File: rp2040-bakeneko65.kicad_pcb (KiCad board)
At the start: 2 copper layers, 303.8 x 94.2 mm, 188 parts, among them J1 SM04B-SRSS-TB, SW1 1u, SW10 1u, SW11 1u, SW12 1u, SW13 1u, SW14 1u, SW15 1u, SW16 1u, SW17 2u, SW18 1.5u, SW19 1u, SW2 1u, SW20 1u, SW21 1u, SW22 1u, SW23 1u, SW24 1u, SW25 1u, SW26 1u, SW27 1u, SW28 1u, SW29 1u, SW3 1u, SW30 1u, SW31 1.5u, SW32 ISO Enter, SW33 1u, SW34 1.25u, SW35 1.75u, SW36 1u, SW37 1u, SW38 1u, SW39 1u, SW4 1u, SW40 1u, SW41 1u, SW42 1u, SW43 1u, SW44 1u, SW45 1u, SW46 1u, SW47 2.25u, SW48 1u, SW49 1u, SW5 1u, SW50 2.25u, SW51 1.25u, SW52 1u, SW53 1u, SW54 1u, SW55 1u, SW56 1u, SW57 1u, SW58 1u, SW59 1u, SW6 1u, SW60 1u, SW61 1u, SW62 1u, SW63 1.75u, SW64 1u, SW65 1u, SW66 1.5u, SW67 1.25u, SW68 1u, SW69 1.25u, SW7 1u, SW70 1.5u, SW71 1.25u, SW72 3u, SW73 7u, SW74 6.25u, SW75 3u, SW76 1.25u, SW77 1.5u, SW78 1.25u, SW79 1u, SW8 1u, SW80 1u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

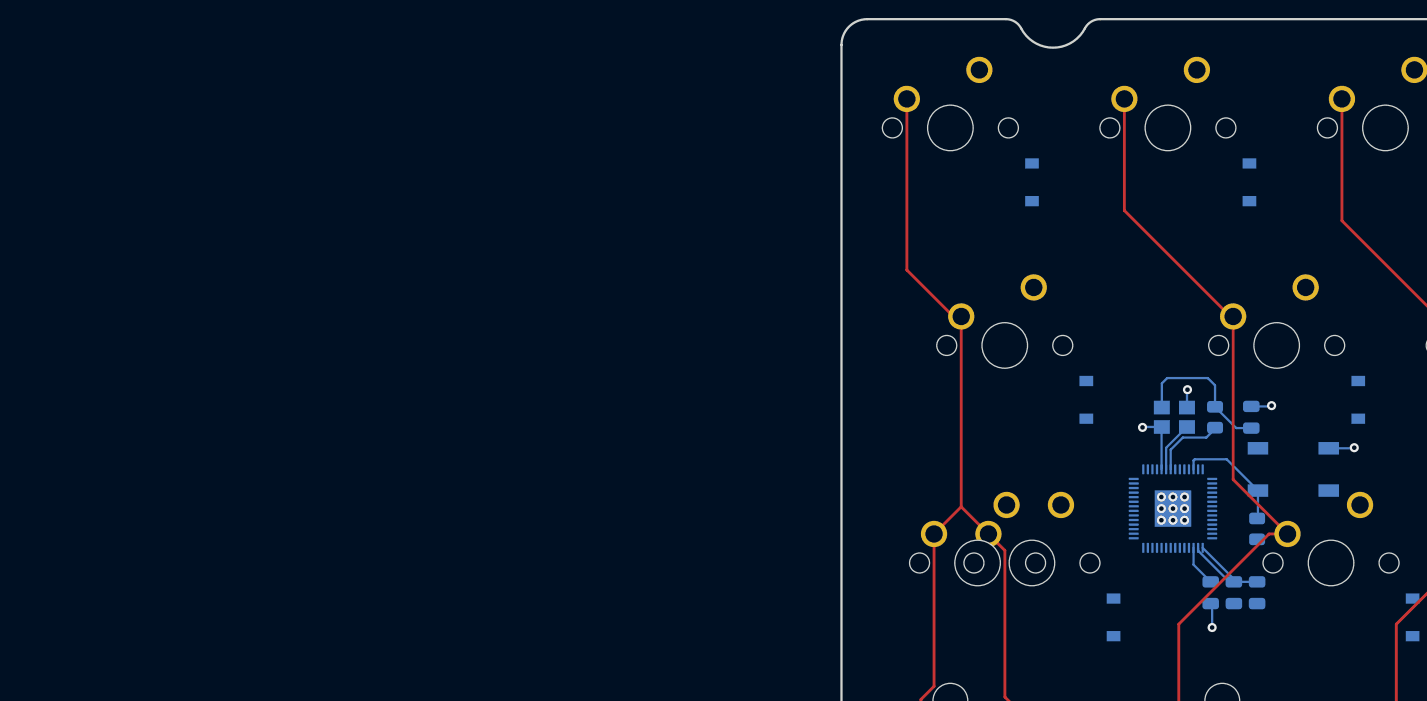
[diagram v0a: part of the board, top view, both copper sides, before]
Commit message: starting over on MCU routing
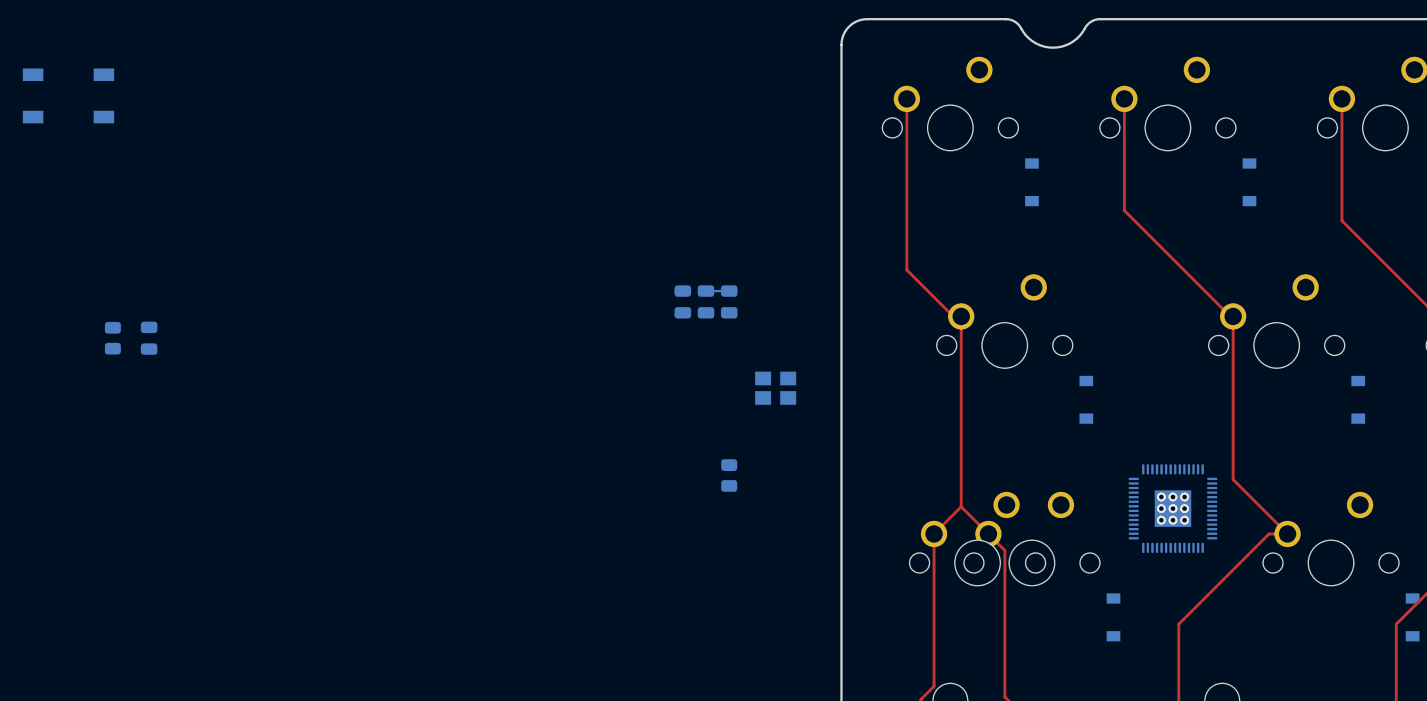
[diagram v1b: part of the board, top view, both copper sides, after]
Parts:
- moved SW83 112.1 mm to (-24.8, 97.2)
- moved C3 96.8 mm to (-17.8, 118.4)
- moved R4 96.8 mm to (-21.0, 118.4)
- moved C11 52.8 mm to (33.0, 115.2)
- moved C10 52.8 mm to (31.0, 115.2)
- moved C6 52.8 mm to (29.0, 115.2)
- moved R3 46.5 mm to (33.0, 130.5)
- moved Y1 35.0 mm to (37.1, 122.8)
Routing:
- net GND: track 14.1 -> 0.00 mm, vias 14 -> 9
- net Net-(C3-Pad2): track 13.3 -> 0.00 mm
- net Net-(R3-Pad2): track 10.2 -> 0.03 mm
- net +3V3: track 10.6 -> 2.44 mm
- net XTAL_OUT: track 6.46 -> 0.00 mm
- net XTAL_IN: track 4.47 -> 0.00 mm
- net +1V1: track 3.60 -> 0.00 mm

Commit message: Use smaller caps and resistors
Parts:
- C1, C10, C11, C12, C13, C14, C15, C16, C17, C2, C3, C4, C5, C6, C7, C8, C9: footprint Capacitor_SMD:C_0805_2012Metric -> Capacitor_SMD:C_0402_1005Metric
- R1, R2, R3, R4: footprint Resistor_SMD:R_0805_2012Metric -> Resistor_SMD:R_0402_1005Metric
- moved R3 60.7 mm to (-24.1, 110.0)
- moved C3 46.1 mm to (27.9, 124.4)
- moved R4 6.64 mm to (-27.6, 119.1)

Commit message: Reposition crystal
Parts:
- moved C2 414.5 mm to (75.9, 139.4), turned to -90 degrees
- moved R4 98.8 mm to (69.1, 139.4), turned to 90 degrees
- moved Y1 39.5 mm to (72.4, 140.6), turned to 90 degrees
- turned U1 to 180 degrees
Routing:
- net XTAL_IN: track 0.00 -> 5.90 mm
- net XTAL_OUT: track 0.00 -> 4.34 mm
- net Net-(C3-Pad2): track 0.00 -> 3.17 mm
- net GND: track 0.00 -> 2.90 mm
- net COL1: track 94.2 -> 93.2 mm

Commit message: Complete crystal
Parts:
- moved C3 46.0 mm to (69.8, 143.4), turned to 90 degrees
- moved C2 3.99 mm to (76.6, 143.4)
- moved R4 3.05 mm to (72.1, 139.4)
- moved Y1 2.57 mm to (73.3, 143.0), turned to 0 degrees
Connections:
- net Net-(R1-Pad2) renamed /D_P
- net Net-(R2-Pad2) renamed /D_N
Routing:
- net GND: track 2.90 -> 15.0 mm, vias 9 -> 11
- net XTAL_IN: track 5.90 -> 11.0 mm
- net XTAL_OUT: track 4.34 -> 2.17 mm
- net Net-(C3-Pad2): track 3.17 -> 4.85 mm

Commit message: failed attempt to route USB DP/DN
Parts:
- moved R2 439.6 mm to (82.2, 109.9)
- moved J1 436.1 mm to (109.6, 110.4), turned to -90 degrees
- moved R1 412.6 mm to (82.2, 110.9)
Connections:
- J1 pad 2: D+ -> D-
- J1 pad 3: D- -> D+
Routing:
- net D-: track 0.00 -> 25.2 mm
- net D+: track 0.00 -> 25.2 mm
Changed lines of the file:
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@@
   )
   (footprint "Resistor_SMD:R_0402_1005Metric" (layer "B.Cu")
-    (at 494.4345 127.625 180)
+    (at 82.169 110.871 180)
     (descr "Resistor SMD 0402 (1005 Metric), square (rectangular) end terminal, IPC_7351 nominal, (Body size source: IPC-SM-782 page 72, https://www.pcb-3d.com/wordpress/wp-content/uploads/ipc-sm-782a_amendment_1_and_2.pdf), generated with kicad-footprint-generator")
     (tags "resistor")
@@
   )
   (footprint "Resistor_SMD:R_0402_1005Metric" (layer "B.Cu")
-    (at 518.7 162.02 180)
+    (at 82.169 109.855 180)
     (descr "Resistor SMD 0402 (1005 Metric), square (rectangular) end terminal, IPC_7351 nominal, (Body size source: IPC-SM-782 page 72, https://www.pcb-3d.com/wordpress/wp-content/uploads/ipc-sm-782a_amendment_1_and_2.pdf), generated with kicad-footprint-generator")
     (tags "resistor")
@@
   )
   (footprint "Connector_JST:JST_SH_SM04B-SRSS-TB_1x04-1MP_P1.00mm_Horizontal" (layer "B.Cu")
-    (at 545.42 126.9 180)
+    (at 109.601 110.363 -90)
     (descr "JST SH series connector, SM04B-SRSS-TB (http://www.jst-mfg.com/product/pdf/eng/eSH.pdf), generated with kicad-footprint-generator")
     (tags "connector JST SH top entry")
@@
     (property "Sheetname" "")
     (attr smd)
-    (fp_text reference "J1" (at 0 3.98) (layer "B.SilkS")
-      (effects (font (size 1 1) (thickness 0.15)) (justify mirror))
-    )
-    (fp_text value "SM04B-SRSS-TB" (at 0 -3.98) (layer "B.Fab")
-      (effects (font (size 1 1) (thickness 0.15)) (justify mirror))
-    )
-    (fp_text user "${REFERENCE}" (at 0 0) (layer "B.Fab")
+    (fp_text reference "J1" (at 0 3.98 -270) (layer "B.SilkS")
+      (effects (font (size 1 1) (thickness 0.15)) (justify mirror))
+    )
+    (fp_text value "SM04B-SRSS-TB" (at 0 -3.98 -270) (layer "B.Fab")
+      (effects (font (size 1 1) (thickness 0.15)) (justify mirror))
+    )
+    (fp_text user "${REFERENCE}" (at 0 0 -270) (layer "B.Fab")
       (effects (font (size 1 1) (thickness 0.15)) (justify mirror))
     )
@@
     (fp_line (start -3 -2.575) (end 3 -2.575) (layer "B.Fab") (width 0.1))
     (fp_line (start -3 1.675) (end -3 -2.575) (layer "B.Fab") (width 0.1))
-    (pad "1" smd roundrect (at -1.5 2 180) (size 0.6 1.55) (layers "B.Cu" "B.Paste" "B.Mask") (roundrect_rratio 0.25)
+    (pad "1" smd roundrect (at -1.5 2 270) (size 0.6 1.55) (layers "B.Cu" "B.Paste" "B.Mask") (roundrect_rratio 0.25)
       (net 5 "+5V") (pinfunction "Pin_1") (pintype "passive"))
-    (pad "2" smd roundrect (at -0.5 2 180) (size 0.6 1.55) (layers "B.Cu" "B.Paste" "B.Mask") (roundrect_rratio 0.25)
-      (net 83 "D+") (pinfunction "Pin_2") (pintype "passive"))
-    (pad "3" smd roundrect (at 0.5 2 180) (size 0.6 1.55) (layers "B.Cu" "B.Paste" "B.Mask") (roundrect_rratio 0.25)
-      (net 84 "D-") (pinfunction "Pin_3") (pintype "passive"))
-    (pad "4" smd roundrect (at 1.5 2 180) (size 0.6 1.55) (layers "B.Cu" "B.Paste" "B.Mask") (roundrect_rratio 0.25)
+    (pad "2" smd roundrect (at -0.5 2 270) (size 0.6 1.55) (layers "B.Cu" "B.Paste" "B.Mask") (roundrect_rratio 0.25)
+      (net 84 "D-") (pinfunction "Pin_2") (pintype "passive"))
+    (pad "3" smd roundrect (at 0.5 2 270) (size 0.6 1.55) (layers "B.Cu" "B.Paste" "B.Mask") (roundrect_rratio 0.25)
+      (net 83 "D+") (pinfunction "Pin_3") (pintype "passive"))
+    (pad "4" smd roundrect (at 1.5 2 270) (size 0.6 1.55) (layers "B.Cu" "B.Paste" "B.Mask") (roundrect_rratio 0.25)
       (net 2 "GND") (pinfunction "Pin_4") (pintype "passive"))
-    (pad "MP" smd roundrect (at 2.8 -1.875 180) (size 1.2 1.8) (layers "B.Cu" "B.Paste" "B.Mask") (roundrect_rratio 0.208333)
+    (pad "MP" smd roundrect (at 2.8 -1.875 270) (size 1.2 1.8) (layers "B.Cu" "B.Paste" "B.Mask") (roundrect_rratio 0.208333)
       (net 2 "GND") (pinfunction "MountPin") (pintype "passive"))
-    (pad "MP" smd roundrect (at -2.8 -1.875 180) (size 1.2 1.8) (layers "B.Cu" "B.Paste" "B.Mask") (roundrect_rratio 0.208333)
+    (pad "MP" smd roundrect (at -2.8 -1.875 270) (size 1.2 1.8) (layers "B.Cu" "B.Paste" "B.Mask") (roundrect_rratio 0.208333)
       (net 2 "GND") (pinfunction "MountPin") (pintype "passive"))
     (model "${KICAD6_3DMODEL_DIR}/Connector_JST.3dshapes/JST_SH_SM04B-SRSS-TB_1x04-1MP_P1.00mm_Horizontal.wrl"
@@
   (segment (start 70.601 142.152) (end 72.179 142.152) (width 0.2) (layer "B.Cu") (net 4))
   (segment (start 72.136 139.956) (end 72.179 139.999) (width 0.2) (layer "B.Cu") (net 4))
+  (segment (start 82.961999 110.588001) (end 82.679 110.871) (width 0.2) (layer "B.Cu") (net 83))
+  (segment (start 107.326001 110.588001) (end 82.961999 110.588001) (width 0.2) (layer "B.Cu") (net 83))
+  (segment (start 107.601 110.863) (end 107.326001 110.588001) (width 0.2) (layer "B.Cu") (net 83))
+  (segment (start 82.961999 110.137999) (end 82.679 109.855) (width 0.2) (layer "B.Cu") (net 84))
+  (segment (start 107.326001 110.137999) (end 82.961999 110.137999) (width 0.2) (layer "B.Cu") (net 84))
+  (segment (start 107.601 109.863) (end 107.326001 110.137999) (width 0.2) (layer "B.Cu") (net 84))
   (segment (start 230.04675 172.742) (end 230.06875 172.72) (width 0.2) (layer "B.Cu") (net 87))
   (segment (start 72.082 136.7875) (end 72.082 138.882) (width 0.2) (layer "B.Cu") (net 88))

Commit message: some JST stuff
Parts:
- moved U3 464.6 mm to (70.4, 109.7), turned to 90 degrees
- moved C4 455.5 mm to (69.9, 114.2), turned to 0 degrees
- moved C5 430.3 mm to (69.8, 113.2), turned to 0 degrees
- moved R1 7.78 mm to (74.4, 110.9)
- moved R2 7.78 mm to (74.4, 109.9)
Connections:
- C4 pad 1: +5V -> +3V3
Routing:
- net +5V: track 0.00 -> 37.3 mm
- net /D_N: track 0.00 -> 21.6 mm
- net /D_P: track 0.00 -> 20.3 mm
- net +3V3: track 2.19 -> 18.7 mm
- net D+: track 25.2 -> 32.9 mm
- net D-: track 25.2 -> 32.9 mm
- net GND: track 15.0 -> 19.3 mm, vias 11 -> 13

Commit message: Power and some decoupling caps
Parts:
- moved C13 462.5 mm to (66.2, 130.7)
- moved C12 457.0 mm to (67.6, 126.2), turned to 90 degrees
- moved C6 41.1 mm to (68.6, 126.2), turned to 90 degrees
- moved C11 36.0 mm to (66.2, 129.3), turned to 180 degrees
- moved R2 16.1 mm to (70.5, 125.5), turned to -90 degrees
- moved R1 14.9 mm to (71.5, 125.5), turned to -90 degrees
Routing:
- net /D_N: track 21.6 -> 4.16 mm
- net /D_P: track 20.3 -> 4.18 mm
- net D-: track 32.9 -> 48.1 mm
- net D+: track 32.9 -> 47.3 mm
- net +3V3: track 18.7 -> 30.6 mm
- net GND: track 19.3 -> 25.6 mm, vias 13 -> 16
- net +1V1: track 0.25 -> 3.82 mm

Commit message: Flash
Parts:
- moved U2 469.5 mm to (80.8, 128.1), turned to 90 degrees
- moved C14 447.2 mm to (72.8, 125.5), turned to 90 degrees
- moved C1 417.8 mm to (82.7, 122.3), turned to 90 degrees
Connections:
- C4 pad 1: +3V3 -> +5V
- U1 pad 2: ROW0 -> unconnected-(U1-Pad2)
- U1 pad 3: ROW1 -> unconnected-(U1-Pad3)
- U1 pad 4: ROW2 -> unconnected-(U1-Pad4)
- U1 pad 5: ROW3 -> unconnected-(U1-Pad5)
- U1 pad 6: ROW4 -> unconnected-(U1-Pad6)
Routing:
- net SD3: track 0.00 -> 15.4 mm
- net SD1: track 0.00 -> 13.1 mm
- net QSPI_CLK: track 0.00 -> 13.0 mm
- net CS: track 0.00 -> 12.8 mm
- net SD2: track 0.00 -> 11.5 mm
- net SD0: track 0.00 -> 9.00 mm
- net +3V3: track 30.6 -> 37.0 mm, vias 0 -> 1
- net GND: track 25.6 -> 29.6 mm, vias 16 -> 18
